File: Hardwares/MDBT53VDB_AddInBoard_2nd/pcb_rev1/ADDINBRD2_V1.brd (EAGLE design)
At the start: 25 x 31 mm, 21 parts, among them CN1 IF_4PIN, CN2 IF_4PIN, CN3 IF_2PIN, CN4 IF_2PIN, Q1 DMP2035UFDF-7, Q2 BC817-40QA, SW1 SKRPACE010, U1 SN74AHC1G00DRLR, U2 REF3325AIRSER, U3 MCP6232T-E/MNY

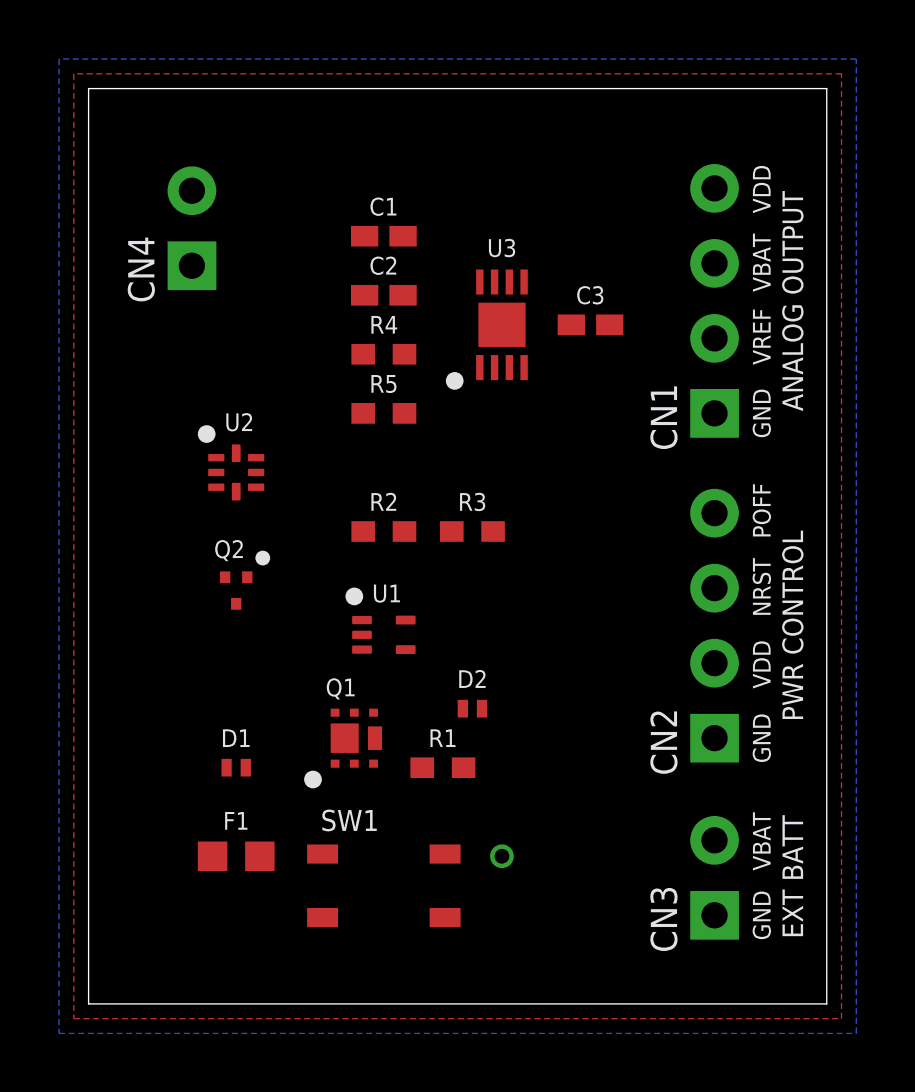
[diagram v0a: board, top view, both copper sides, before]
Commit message: レイアウトを修正
・電圧測定回路の部品配置を修正
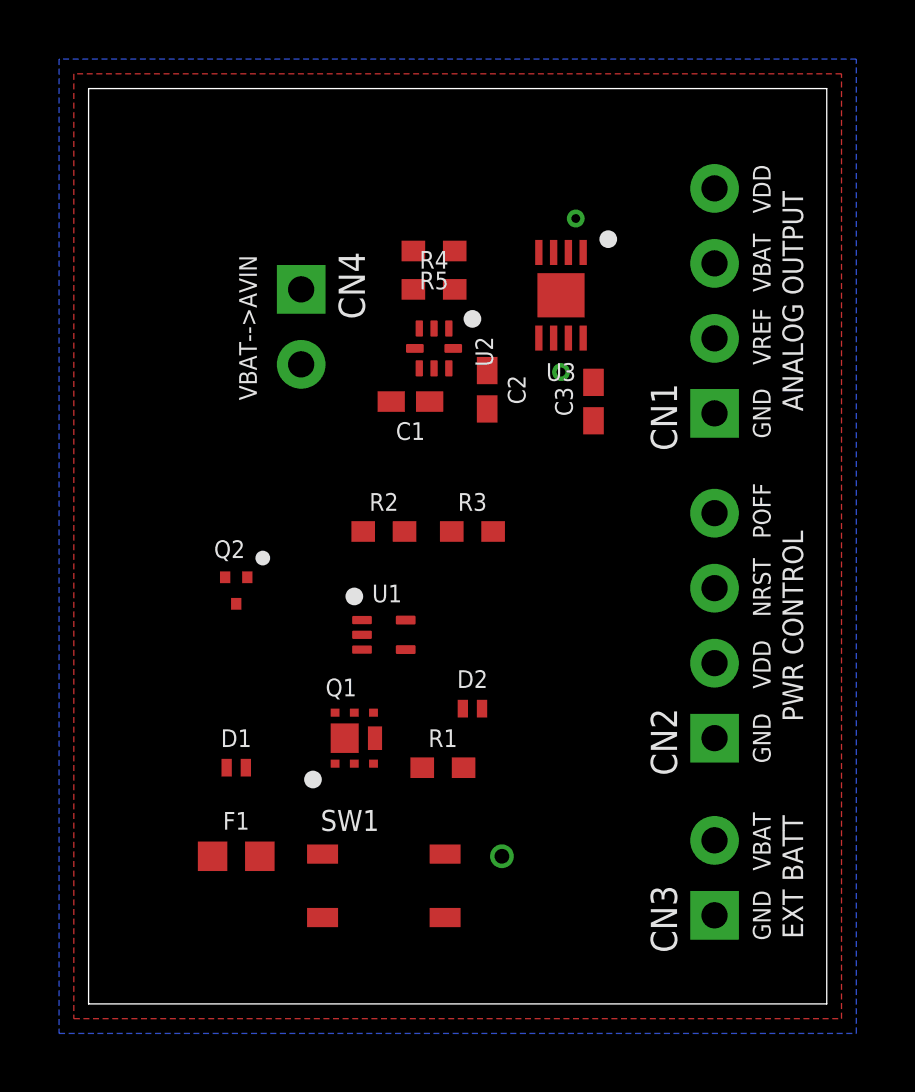
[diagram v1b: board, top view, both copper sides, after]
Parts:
- moved U2 7.91 mm to (11.7, 22.2), turned to 270 degrees
- moved R5 5.76 mm to (11.7, 25.5), turned to 180 degrees
- moved C1 5.67 mm to (10.9, 20.4), turned to 180 degrees
- moved C2 4.74 mm to (13.5, 20.8), turned to 270 degrees
- moved CN4 3.79 mm to (7.20, 24.2), turned to 270 degrees
- moved R4 2.78 mm to (11.7, 24.2)
- moved C3 2.60 mm to (17.1, 20.4), turned to 90 degrees
- moved U3 2.24 mm to (16.0, 24.0), turned to 180 degrees
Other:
- board text added: "VBAT-->AVIN"
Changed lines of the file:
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@@
 <setting verticaltext="up"/>
 </settings>
-<grid distance="0.5" unitdist="mm" unit="mm" style="lines" multiple="1" display="yes" altdistance="0.025" altunitdist="inch" altunit="inch"/>
+<grid distance="0.1" unitdist="mm" unit="mm" style="lines" multiple="1" display="yes" altdistance="0.025" altunitdist="inch" altunit="inch"/>
 <layers>
 <layer number="1" name="Top" color="4" fill="1" visible="yes" active="yes"/>
@@
 <dimension x1="0" y1="0" x2="0" y2="31" x3="-2" y3="15.5" textsize="1.778" layer="51"/>
 <dimension x1="0" y1="31" x2="25" y2="31" x3="12.5" y3="33" textsize="1.778" layer="51"/>
+<text x="5.1" y="22.9" size="0.6" layer="21" rot="R90" align="top-center">VBAT--&gt;AVIN</text>
 </plain>
 <attributes>
@@
 <element name="R2" library="SMDs" package="R0402N" value="5.1k" x="10" y="16"/>
 <element name="R3" library="SMDs" package="R0402N" value="51k" x="13" y="16"/>
-<element name="U2" library="ICs" package="RSE0008A" value="REF3325AIRSER" x="5" y="18"/>
-<element name="C1" library="SMDs" package="C0402" value="1uF" x="10" y="26"/>
-<element name="C2" library="SMDs" package="C0402" value="1uF" x="10" y="24"/>
-<element name="R4" library="SMDs" package="R0402N" value="5.1k" x="10" y="22"/>
-<element name="R5" library="SMDs" package="R0402N" value="15k" x="10" y="20"/>
-<element name="C3" library="SMDs" package="C0402" value="0.1uF" x="17" y="23"/>
+<element name="U2" library="ICs" package="RSE0008A" value="REF3325AIRSER" x="11.7" y="22.2" rot="R270"/>
+<element name="C1" library="SMDs" package="C0402" value="1uF" x="10.9" y="20.4" rot="R180"/>
+<element name="C2" library="SMDs" package="C0402" value="1uF" x="13.5" y="20.8" rot="R270"/>
+<element name="R4" library="SMDs" package="R0402N" value="5.1k" x="11.7" y="24.2"/>
+<element name="R5" library="SMDs" package="R0402N" value="15k" x="11.7" y="25.5" rot="R180"/>
+<element name="C3" library="SMDs" package="C0402" value="0.1uF" x="17.1" y="20.4" rot="R90"/>
 <element name="Q1" library="SMDs" package="U-DFN2020-6" value="DMP2035UFDF-7" x="9" y="9"/>
 <element name="Q2" library="SMDs" package="DFN1010D-3" value="BC817-40QA" x="5" y="14"/>
 <element name="U1" library="ICs" package="DRL0005A" value="SN74AHC1G00DRLR" x="10" y="12.5"/>
-<element name="U3" library="ICs" package="TDFN-2X3" value="MCP6232T-E/MNY" x="14" y="23"/>
+<element name="U3" library="ICs" package="TDFN-2X3" value="MCP6232T-E/MNY" x="16" y="24" rot="R180"/>
 <element name="CN1" library="Connectors" package="HEADER_4PIN" value="IF_4PIN" x="21.2" y="20" rot="R90"/>
 <element name="CN2" library="Connectors" package="HEADER_4PIN" value="IF_4PIN" x="21.2" y="9" rot="R90"/>
 <element name="CN3" library="Connectors" package="HEADER_2PIN" value="IF_2PIN" x="21.2" y="3" rot="R90"/>
-<element name="CN4" library="Connectors" package="HEADER_2PIN" value="IF_2PIN" x="3.5" y="25" rot="R90"/>
+<element name="CN4" library="Connectors" package="HEADER_2PIN" value="IF_2PIN" x="7.2" y="24.2" rot="R270"/>
 </elements>
 <signals>
@@
 <contactref element="CN3" pad="1"/>
 <contactref element="CN2" pad="1"/>
-<wire x1="14" y1="23" x2="14.75" y2="21.55" width="0" layer="19" extent="1-1"/>
-<wire x1="5" y1="17.35" x2="4.625" y2="14.45" width="0" layer="19" extent="1-1"/>
+<wire x1="16" y1="24" x2="15.25" y2="25.45" width="0" layer="19" extent="1-1"/>
+<wire x1="11.05" y1="22.2" x2="10.25" y2="20.4" width="0" layer="19" extent="1-1"/>
 <wire x1="9.26" y1="12" x2="12.3" y2="16" width="0" layer="19" extent="1-1"/>
 </signal>
@@
 <wire x1="13.325" y1="10" x2="21.2" y2="11.54" width="0" layer="19" extent="1-1"/>
 <wire x1="10.74" y1="13" x2="13.325" y2="10" width="0" layer="19" extent="1-1"/>
-<wire x1="3.5" y1="27.54" x2="10.74" y2="13" width="0" layer="19" extent="1-1"/>
+<wire x1="7.2" y1="21.66" x2="10.74" y2="13" width="0" layer="19" extent="1-1"/>
 </signal>
 <signal name="EXT_BAT">
@@
 <contactref element="C2" pad="1"/>
 <contactref element="U3" pad="5"/>
-<wire x1="9.35" y1="24" x2="14.75" y2="24.45" width="0" layer="19" extent="1-1"/>
-<wire x1="5" y1="18.65" x2="9.35" y2="24" width="0" layer="19" extent="1-1"/>
+<wire x1="13.5" y1="21.45" x2="15.25" y2="22.55" width="0" layer="19" extent="1-1"/>
+<wire x1="12.35" y1="22.2" x2="13.5" y2="21.45" width="0" layer="19" extent="1-1"/>
 </signal>
 <signal name="AVBAT_IN">
@@
 <contactref element="R5" pad="1"/>
 <contactref element="U3" pad="3"/>
-<wire x1="10.7" y1="22" x2="14.25" y2="21.55" width="0" layer="19" extent="1-1"/>
-<wire x1="9.3" y1="20" x2="10.7" y2="22" width="0" layer="19" extent="1-1"/>
+<wire x1="12.4" y1="25.5" x2="15.75" y2="25.45" width="0" layer="19" extent="1-1"/>
+<wire x1="12.4" y1="24.2" x2="12.4" y2="25.5" width="0" layer="19" extent="1-1"/>
 </signal>
 <signal name="N$2">
@@
 <contactref element="U3" pad="2"/>
 <contactref element="CN1" pad="3"/>
-<wire x1="13.75" y1="21.55" x2="21.2" y2="25.08" width="0" layer="19" extent="1-1"/>
-<wire x1="13.25" y1="21.55" x2="13.75" y2="21.55" width="0" layer="19" extent="1-1"/>
+<via x="16.5" y="26.6" extent="1-16" drill="0.3"/>
+<wire x1="16.75" y1="25.45" x2="21.2" y2="25.08" width="0" layer="19" extent="1-1"/>
+<wire x1="16.25" y1="25.45" x2="16.75" y2="25.45" width="0" layer="19" extent="1-1"/>
+<wire x1="16.5" y1="26.6" x2="16.75" y2="25.45" width="0" layer="19" extent="1-1"/>
 </signal>
 <signal name="AVREF">
@@
 <contactref element="U3" pad="6"/>
 <contactref element="CN1" pad="2"/>
-<wire x1="14.25" y1="24.45" x2="21.2" y2="22.54" width="0" layer="19" extent="1-1"/>
-<wire x1="13.75" y1="24.45" x2="14.25" y2="24.45" width="0" layer="19" extent="1-1"/>
+<via x="16" y="21.4" extent="1-16" drill="0.3"/>
+<wire x1="16.25" y1="22.55" x2="21.2" y2="22.54" width="0" layer="19" extent="1-1"/>
+<wire x1="15.75" y1="22.55" x2="16.25" y2="22.55" width="0" layer="19" extent="1-1"/>
+<wire x1="16" y1="21.4" x2="16.25" y2="22.55" width="0" layer="19" extent="1-1"/>
 </signal>
 <signal name="AVIN">
@@
 <contactref element="U3" pad="8"/>
 <contactref element="CN4" pad="1"/>
-<wire x1="16.35" y1="23" x2="21.2" y2="27.62" width="0" layer="19" extent="1-1"/>
-<wire x1="13.25" y1="24.45" x2="16.35" y2="23" width="0" layer="19" extent="1-1"/>
-<wire x1="9.35" y1="26" x2="13.25" y2="24.45" width="0" layer="19" extent="1-1"/>
-<wire x1="9.3" y1="22" x2="9.35" y2="26" width="0" layer="19" extent="1-1"/>
-<wire x1="5.675" y1="17.5" x2="9.3" y2="22" width="0" layer="19" extent="1-1"/>
-<wire x1="3.5" y1="25" x2="9.35" y2="26" width="0" layer="19" extent="1-1"/>
+<wire x1="16.75" y1="22.55" x2="21.2" y2="27.62" width="0" layer="19" extent="1-1"/>
+<wire x1="17.1" y1="19.75" x2="16.75" y2="22.55" width="0" layer="19" extent="1-1"/>
+<wire x1="11.55" y1="20.4" x2="17.1" y2="19.75" width="0" layer="19" extent="1-1"/>
+<wire x1="11.2" y1="21.525" x2="11.55" y2="20.4" width="0" layer="19" extent="1-1"/>
+<wire x1="11" y1="24.2" x2="11.2" y2="21.525" width="0" layer="19" extent="1-1"/>
+<wire x1="7.2" y1="24.2" x2="11" y2="24.2" width="0" layer="19" extent="1-1"/>
 </signal>
 </signals>

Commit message: レイアウトを修正
・電源遮断回路の部品配置を修正
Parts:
- moved Q2 8.56 mm to (13.5, 15.0)
- moved U1 6.96 mm to (16.5, 15.0), turned to 180 degrees
- moved R2 5.10 mm to (15.0, 17.0), turned to 180 degrees
- moved R3 1.41 mm to (12.0, 17.0)
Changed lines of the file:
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@@
 <element name="R1" library="SMDs" package="R0402N" value="5.1k" x="12" y="8"/>
 <element name="D2" library="SMDs" package="DSN1006-2" value="PMEG4010AESBYL" x="13" y="10"/>
-<element name="R2" library="SMDs" package="R0402N" value="5.1k" x="10" y="16"/>
-<element name="R3" library="SMDs" package="R0402N" value="51k" x="13" y="16"/>
+<element name="R2" library="SMDs" package="R0402N" value="5.1k" x="15" y="17" smashed="yes" rot="R180">
+<attribute name="NAME" x="15" y="17.7" size="0.6" layer="25" align="bottom-center"/>
+<attribute name="VALUE" x="15" y="17.8" size="0.6" layer="27" rot="R180" align="top-center"/>
+</element>
+<element name="R3" library="SMDs" package="R0402N" value="51k" x="12" y="17"/>
 <element name="U2" library="ICs" package="RSE0008A" value="REF3325AIRSER" x="11.7" y="22.2" rot="R270"/>
 <element name="C1" library="SMDs" package="C0402" value="1uF" x="10.9" y="20.4" rot="R180"/>
@@
 <element name="C3" library="SMDs" package="C0402" value="0.1uF" x="17.1" y="20.4" rot="R90"/>
 <element name="Q1" library="SMDs" package="U-DFN2020-6" value="DMP2035UFDF-7" x="9" y="9"/>
-<element name="Q2" library="SMDs" package="DFN1010D-3" value="BC817-40QA" x="5" y="14"/>
-<element name="U1" library="ICs" package="DRL0005A" value="SN74AHC1G00DRLR" x="10" y="12.5"/>
+<element name="Q2" library="SMDs" package="DFN1010D-3" value="BC817-40QA" x="13.5" y="15" smashed="yes">
+<attribute name="VALUE" x="13" y="13.5" size="0.6" layer="27"/>
+<attribute name="NAME" x="11.9" y="14.8" size="0.6" layer="25" align="bottom-center"/>
+</element>
+<element name="U1" library="ICs" package="DRL0005A" value="SN74AHC1G00DRLR" x="16.5" y="15" rot="R180"/>
 <element name="U3" library="ICs" package="TDFN-2X3" value="MCP6232T-E/MNY" x="16" y="24" rot="R180"/>
 <element name="CN1" library="Connectors" package="HEADER_4PIN" value="IF_4PIN" x="21.2" y="20" rot="R90"/>
@@
 <wire x1="16" y1="24" x2="15.25" y2="25.45" width="0" layer="19" extent="1-1"/>
 <wire x1="11.05" y1="22.2" x2="10.25" y2="20.4" width="0" layer="19" extent="1-1"/>
-<wire x1="9.26" y1="12" x2="12.3" y2="16" width="0" layer="19" extent="1-1"/>
+<wire x1="17.24" y1="15.5" x2="13.125" y2="15.45" width="0" layer="19" extent="1-1"/>
 </signal>
 <signal name="N$1">
@@
 <contactref element="Q2" pad="3"/>
 <contactref element="Q1" pad="3"/>
+<wire x1="11.3" y1="8" x2="13.5" y2="14.55" width="0" layer="19" extent="1-1"/>
 <wire x1="9.65" y1="8.137" x2="11.3" y2="8" width="0" layer="19" extent="1-1"/>
 <wire x1="12.075" y1="2.925" x2="11.3" y2="8" width="0" layer="19" extent="1-1"/>
 <wire x1="7.925" y1="2.925" x2="12.075" y2="2.925" width="0" layer="19" extent="1-1"/>
-<wire x1="5" y1="13.55" x2="9.65" y2="8.137" width="0" layer="19" extent="1-1"/>
 </signal>
 <signal name="VIN">
@@
 <contactref element="CN2" pad="2"/>
 <contactref element="CN4" pad="2"/>
-<wire x1="13.325" y1="10" x2="21.2" y2="11.54" width="0" layer="19" extent="1-1"/>
-<wire x1="10.74" y1="13" x2="13.325" y2="10" width="0" layer="19" extent="1-1"/>
-<wire x1="7.2" y1="21.66" x2="10.74" y2="13" width="0" layer="19" extent="1-1"/>
+<wire x1="15.76" y1="14.5" x2="21.2" y2="11.54" width="0" layer="19" extent="1-1"/>
+<wire x1="13.325" y1="10" x2="15.76" y2="14.5" width="0" layer="19" extent="1-1"/>
+<wire x1="7.2" y1="21.66" x2="15.76" y2="14.5" width="0" layer="19" extent="1-1"/>
 </signal>
 <signal name="EXT_BAT">
@@
 <contactref element="R3" pad="2"/>
 <contactref element="Q2" pad="1"/>
-<wire x1="10.7" y1="16" x2="13.7" y2="16" width="0" layer="19" extent="1-1"/>
-<wire x1="5.375" y1="14.45" x2="10.7" y2="16" width="0" layer="19" extent="1-1"/>
+<wire x1="12.7" y1="17" x2="14.3" y2="17" width="0" layer="19" extent="1-1"/>
+<wire x1="13.875" y1="15.45" x2="14.3" y2="17" width="0" layer="19" extent="1-1"/>
 </signal>
 <signal name="AVREF_IN">
@@
 <contactref element="U1" pad="4"/>
 <contactref element="R2" pad="1"/>
-<wire x1="10.74" y1="12" x2="9.3" y2="16" width="0" layer="19" extent="1-1"/>
+<wire x1="15.7" y1="17" x2="15.76" y2="15.5" width="0" layer="19" extent="1-1"/>
 </signal>
 <signal name="NRST">
 <contactref element="U1" pad="2"/>
 <contactref element="CN2" pad="3"/>
-<wire x1="9.26" y1="12.5" x2="21.2" y2="14.08" width="0" layer="19" extent="1-1"/>
+<wire x1="17.24" y1="15" x2="21.2" y2="14.08" width="0" layer="19" extent="1-1"/>
 </signal>
 <signal name="PWR_OFF">
 <contactref element="U1" pad="1"/>
 <contactref element="CN2" pad="4"/>
-<wire x1="9.26" y1="13" x2="21.2" y2="16.62" width="0" layer="19" extent="1-1"/>
+<wire x1="17.24" y1="14.5" x2="21.2" y2="16.62" width="0" layer="19" extent="1-1"/>
 </signal>
 <signal name="AVBAT">
